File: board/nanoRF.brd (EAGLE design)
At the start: 22.9 x 49.5 mm, 19 parts

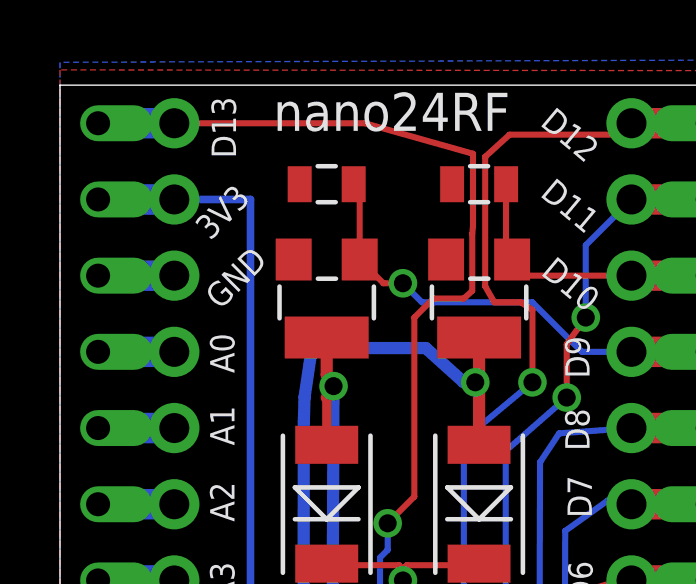
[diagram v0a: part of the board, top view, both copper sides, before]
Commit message: changed prj name and files to nanoRF, starting fix for AREF pin
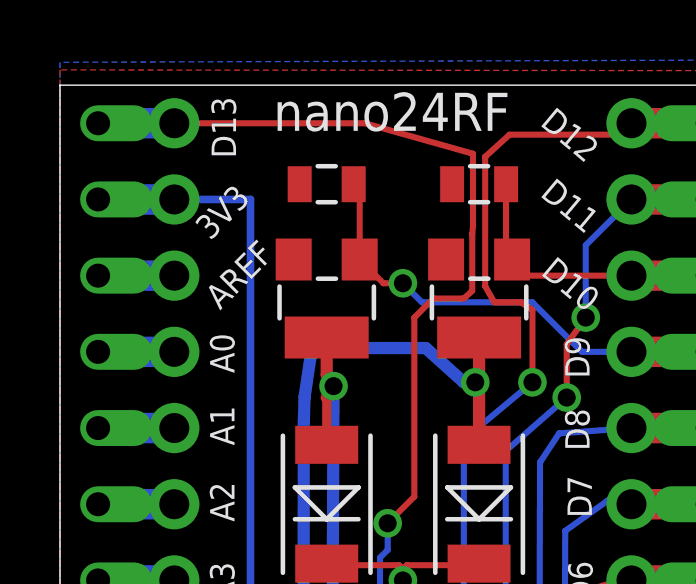
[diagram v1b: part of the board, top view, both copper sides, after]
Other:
- board text added: "AREF"
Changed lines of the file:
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@@
 <?xml version="1.0" encoding="utf-8"?>
 <!DOCTYPE eagle SYSTEM "eagle.dtd">
-<eagle version="8.0.0">
+<eagle version="7.6.0">
 <drawing>
 <settings>
@@
 <text x="3.2766" y="37.5186" size="0.8128" layer="21" rot="SR90">A1</text>
 <text x="3.2766" y="39.9316" size="0.8128" layer="21" rot="SR90">A0</text>
-<text x="2.794" y="42.0144" size="0.8128" layer="21" rot="R45">GND</text>
+<text x="2.794" y="42.0144" size="0.8128" layer="21" rot="R45">AREF</text>
 <text x="2.4638" y="44.3258" size="0.8128" layer="21" rot="R45">3V3</text>
 <text x="3.3274" y="47.0944" size="0.8128" layer="21" rot="SR90">D13</text>

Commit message: fixed Aref pin horror
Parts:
- removed JP1: (no value), nano24rf:1X15_ROUND_70
- removed JP4: (no value), nano24rf:1X15_LONG
- added U$11: HEADER_1X2ROUND, nanoRF:1X2_ROUND_70
- added U$6: HEADER-1X12LONG, nanoRF:1X12_LONG
- added U$7: HEADER-1X12ROUND, nanoRF:1X12_ROUND_70
- added U$8: HEADER_1X2LONG, nanoRF:1X2_LONG
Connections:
- net 3V3: now also U$11.2, U$8.P$2; no longer JP1.2, JP4.P$2
- net GND: now also U$6.P$11, U$7.11; no longer JP1.14, JP1.3, JP4.P$14, JP4.P$3
- net N$1: now also U$6.P$1, U$7.1; no longer JP1.4, JP4.P$4
- net N$10: now also U$6.P$10, U$7.10; no longer JP1.13, JP4.P$13
- net N$2: now also U$6.P$2, U$7.2; no longer JP1.5, JP4.P$5
- net N$3: now also U$6.P$3, U$7.3; no longer JP1.6, JP4.P$6
- net N$4: now also U$6.P$4, U$7.4; no longer JP1.7, JP4.P$7
- net N$5: now also U$6.P$5, U$7.5; no longer JP1.8, JP4.P$8
- net N$6: now also U$6.P$6, U$7.6; no longer JP1.9, JP4.P$9
- net N$7: now also U$6.P$7, U$7.7; no longer JP1.10, JP4.P$10
- net N$8: now also U$6.P$8, U$7.8; no longer JP1.11, JP4.P$11
- net N$9: now also U$6.P$9, U$7.9; no longer JP1.12, JP4.P$12
- net SCK: now also U$11.1, U$8.P$1; no longer JP1.1, JP4.P$1
- net VIN: now also U$6.P$12, U$7.12; no longer JP1.15, JP4.P$15
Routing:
- net GND: track 23.7 -> 19.9 mm
- net 3V3: track 48.1 -> 44.3 mm
- net N$9: track 2.54 -> 1.27 mm
- net N$8: track 2.54 -> 1.27 mm
- net N$7: track 2.54 -> 1.27 mm
- net N$6: track 2.54 -> 1.27 mm
- net N$5: track 2.54 -> 1.27 mm
- net N$4: track 2.54 -> 1.27 mm
- net N$3: track 2.54 -> 1.27 mm
- net N$2: track 2.54 -> 1.27 mm
- net N$10: track 2.54 -> 1.27 mm
- net N$1: track 2.54 -> 1.27 mm
- net VIN: track 25.3 -> 24.0 mm
- net SCK: track 56.5 -> 55.2 mm
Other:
- board text added: "nanoRF"

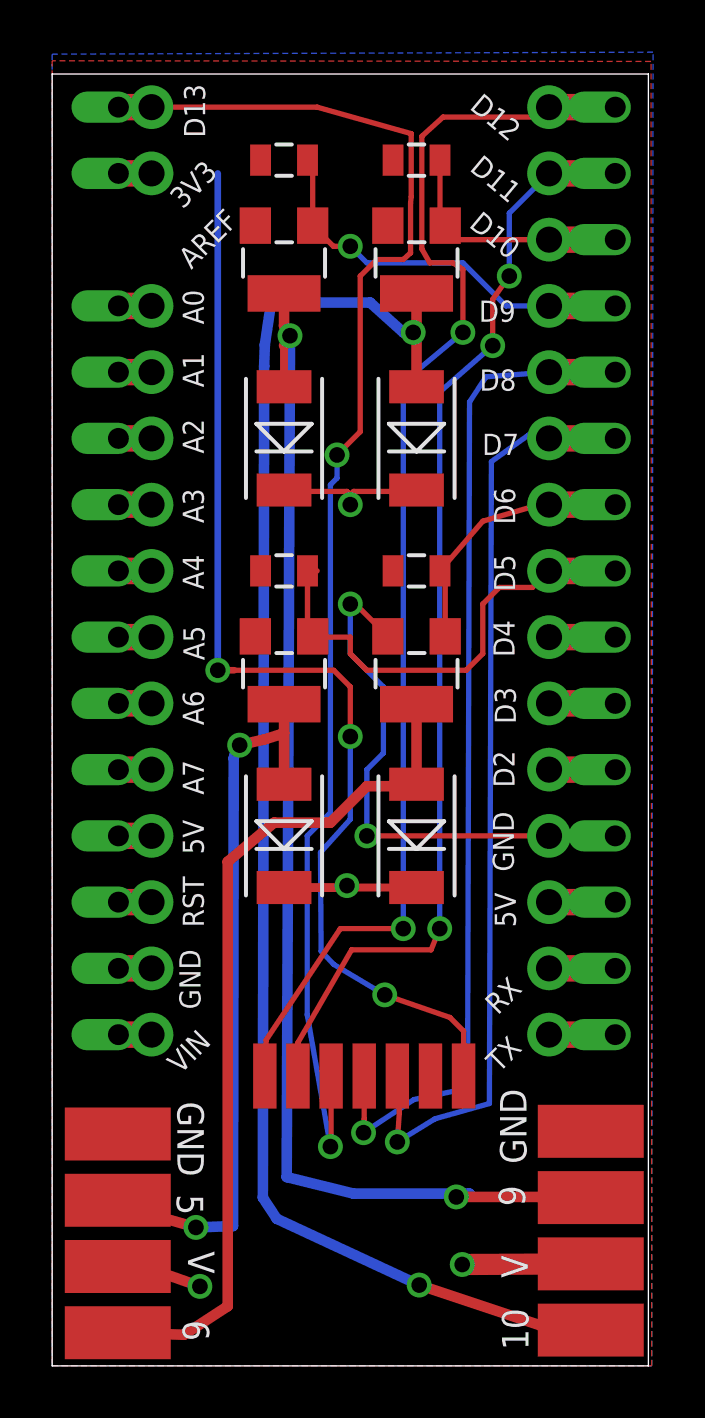
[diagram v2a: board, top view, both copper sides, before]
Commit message: removed reset and aref
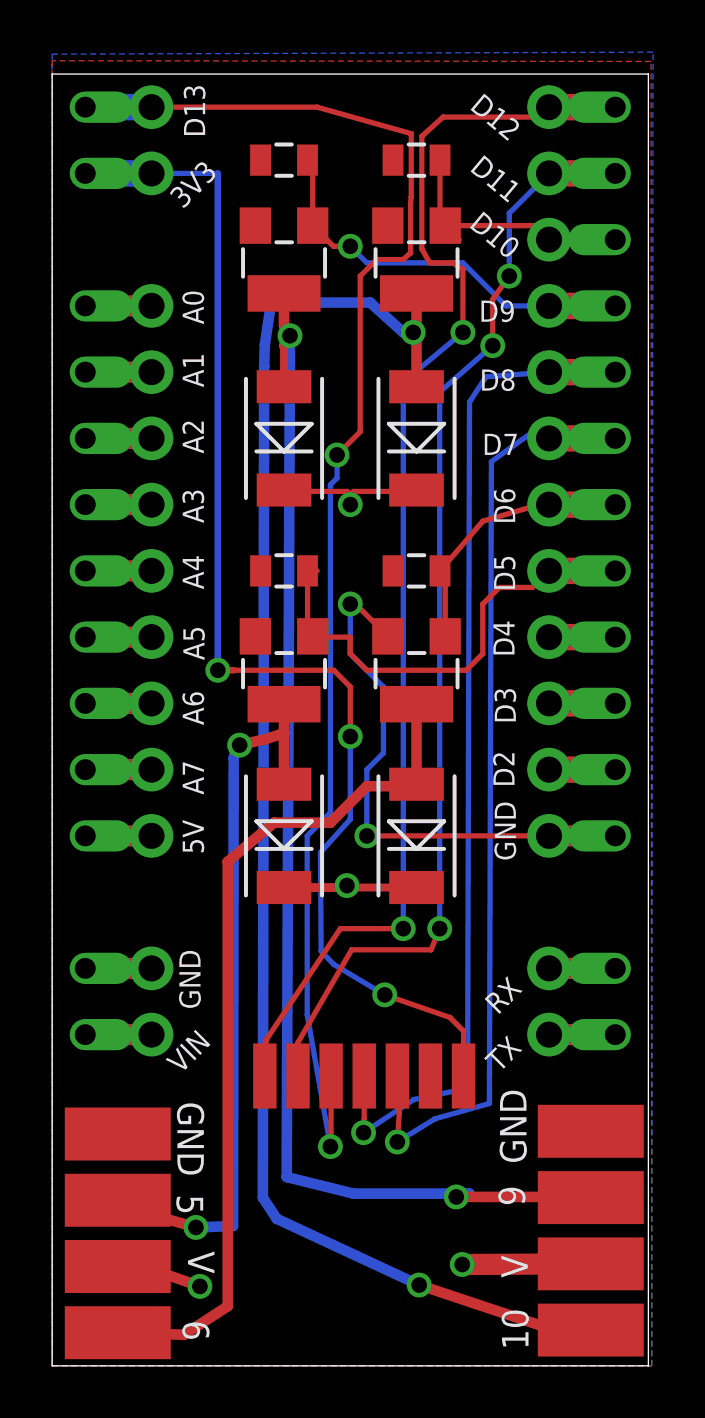
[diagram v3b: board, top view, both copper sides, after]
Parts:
- removed JP2: (no value), nano24rf:1X15_ROUND_70
- removed JP3: (no value), nano24rf:1X15_LONG
- added U$12, U$16: HEADER_1X2ROUND, nanoRF:1X2_ROUND_70
- added U$13, U$15: HEADER_1X2LONG, nanoRF:1X2_LONG
- added U$14: HEADER-1X12LONG, nanoRF:1X12_LONG
- added U$18: HEADER-1X12ROUND, nanoRF:1X12_ROUND_70
- U$6: value HEADER-1X12LONG -> HEADER-1X09RND; device nanoRF:1X12_LONG -> nanoRF:1X09_ROUND_70
- U$7: value HEADER-1X12ROUND -> HEADER-1X09LONG; device nanoRF:1X12_ROUND_70 -> nanoRF:1X09_LONG
- moved U$7 4.58 mm to (-1.27, 30.5), turned to 90 degrees
- moved U$6 4.02 mm to (1.27, 30.5), turned to 90 degrees
- moved U$8 1.27 mm to (-1.27, 47.0), flipped to the bottom
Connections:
- removed net N$10: U$6.P$10, U$7.10
- removed net N$13: JP2.13, JP3.P$3
- net CE: now also U$14.P$6, U$18.6; no longer JP2.6, JP3.P$10
- net CSN: now also U$14.P$5, U$18.5; no longer JP2.5, JP3.P$11
- net D10: now also U$14.P$3, U$18.3; no longer JP2.3, JP3.P$13
- net D5: now also U$14.P$8, U$18.8; no longer JP2.8, JP3.P$8
- net D6: now also U$14.P$7, U$18.7; no longer JP2.7, JP3.P$9
- net D9: now also U$14.P$4, U$18.4; no longer JP2.4, JP3.P$12
- net GND: now also U$12.1, U$13.P$1, U$14.P$12, U$18.12; no longer JP2.12, JP3.P$4, U$6.P$11, U$7.11
- net MISO: now also U$14.P$1, U$18.1; no longer JP2.1, JP3.P$15
- net MOSI: now also U$14.P$2, U$18.2; no longer JP2.2, JP3.P$14
- net N$1: now also U$6.1, U$7.P$1; no longer U$6.P$1, U$7.1
- net N$11: now also U$15.P$2, U$16.2; no longer JP2.15, JP3.P$1
- net N$12: now also U$15.P$1, U$16.1; no longer JP2.14, JP3.P$2
- net N$14: now also U$14.P$11, U$18.11; no longer JP2.11, JP3.P$5
- net N$15: now also U$14.P$10, U$18.10; no longer JP2.10, JP3.P$6
- net N$16: now also U$14.P$9, U$18.9; no longer JP2.9, JP3.P$7
- net N$2: now also U$6.2, U$7.P$2; no longer U$6.P$2, U$7.2
- net N$3: now also U$6.3, U$7.P$3; no longer U$6.P$3, U$7.3
- net N$4: now also U$6.4, U$7.P$4; no longer U$6.P$4, U$7.4
- net N$5: now also U$6.5, U$7.P$5; no longer U$6.P$5, U$7.5
- net N$6: now also U$6.6, U$7.P$6; no longer U$6.P$6, U$7.6
- net N$7: now also U$6.7, U$7.P$7; no longer U$6.P$7, U$7.7
- net N$8: now also U$6.8, U$7.P$8; no longer U$6.P$8, U$7.8
- net N$9: now also U$6.9, U$7.P$9; no longer U$6.P$9, U$7.9
- net VIN: now also U$12.2, U$13.P$2; no longer U$6.P$12, U$7.12
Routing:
- net GND: track 19.9 -> 23.7 mm
- net 3V3: track 44.3 -> 48.1 mm
- net N$13: track 2.54 -> 0.00 mm
- net N$9: track 1.27 -> 2.54 mm
- net N$8: track 1.27 -> 2.54 mm
- net N$7: track 1.27 -> 2.54 mm
- net N$6: track 1.27 -> 2.54 mm
- net N$5: track 1.27 -> 2.54 mm
- net N$4: track 1.27 -> 2.54 mm
- net N$3: track 1.27 -> 2.54 mm
- net N$2: track 1.27 -> 2.54 mm
- net N$10: track 1.27 -> 0.00 mm
- net N$1: track 1.27 -> 2.54 mm
- net VIN: track 24.0 -> 25.3 mm
- net SCK: track 55.2 -> 56.5 mm
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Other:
- board text removed: "AREF"
- board text removed: "RST"
